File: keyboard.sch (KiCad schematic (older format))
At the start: 65 parts, among them J1 USB_A, SW1 KEY_ESC, SW10 KEY_LSPECIAL, SW11 KEY_2, SW12 KEY_W, SW13 KEY_S, SW14 KEY_X, SW15 KEY_LALT, SW16 KEY_3, SW17 KEY_E, SW18 KEY_D, SW19 KEY_C, SW2 KEY_TAB, SW20 KEY_SPACE, SW21 KEY_4, SW22 KEY_R, SW23 KEY_F, SW24 KEY_V, SW25 KEY_RALT, SW26 KEY_5, SW27 KEY_T, SW28 KEY_G, SW29 KEY_B, SW3 KEY_CAPS, SW30 KEY_RSPECIAL, SW31 KEY_6, SW32 KEY_Y, SW33 KEY_H, SW34 KEY_N, SW35 KEY_FN, SW36 KEY_7, SW37 KEY_U, SW38 KEY_J, SW39 KEY_M, SW4 KEY_LSHIFT, SW40 KEY_RCTRL, SW41 KEY_8, SW42 KEY_I, SW43 KEY_K, SW44 KEY_COMMA, SW45 KEY_9, SW46 KEY_O, SW47 KEY_L, SW48 KEY_PERIOD, SW49 KEY_0, SW5 KEY_LCTRL, SW50 KEY_P, SW51 KEY_SEMI, SW52 KEY_SLASH, SW53 KEY_MINUS, SW54 KEY_LBRACK, SW55 KEY_APOS, SW56 KEY_RSHIFT, SW57 KEY_EQUAL, SW58 KEY_RBRACK, SW59 KEY_ENTER, SW6 KEY_1, SW60 KEY_BKSPACE, SW61 KEY_BKSLSH, SW7 KEY_Q, SW8 KEY_A, SW9 KEY_Z, Y1 16mhz

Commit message: More routing
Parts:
- removed SW1: KEY_ESC, symbol CHERRYMX
- removed SW10: KEY_LSPECIAL, symbol CHERRYMX
- removed SW11: KEY_2, symbol CHERRYMX
- removed SW12: KEY_W, symbol CHERRYMX
- removed SW13: KEY_S, symbol CHERRYMX
- removed SW14: KEY_X, symbol CHERRYMX
- removed SW15: KEY_LALT, symbol CHERRYMX
- removed SW16: KEY_3, symbol CHERRYMX
- removed SW17: KEY_E, symbol CHERRYMX
- removed SW18: KEY_D, symbol CHERRYMX
- removed SW19: KEY_C, symbol CHERRYMX
- removed SW2: KEY_TAB, symbol CHERRYMX
- removed SW20: KEY_SPACE, symbol CHERRYMX
- removed SW21: KEY_4, symbol CHERRYMX
- removed SW22: KEY_R, symbol CHERRYMX
- removed SW23: KEY_F, symbol CHERRYMX
- removed SW24: KEY_V, symbol CHERRYMX
- removed SW25: KEY_RALT, symbol CHERRYMX
- removed SW26: KEY_5, symbol CHERRYMX
- removed SW27: KEY_T, symbol CHERRYMX
- removed SW28: KEY_G, symbol CHERRYMX
- removed SW29: KEY_B, symbol CHERRYMX
- removed SW3: KEY_CAPS, symbol CHERRYMX
- removed SW30: KEY_RSPECIAL, symbol CHERRYMX
- removed SW31: KEY_6, symbol CHERRYMX
- removed SW32: KEY_Y, symbol CHERRYMX
- removed SW33: KEY_H, symbol CHERRYMX
- removed SW34: KEY_N, symbol CHERRYMX
- removed SW35: KEY_FN, symbol CHERRYMX
- removed SW36: KEY_7, symbol CHERRYMX
- removed SW37: KEY_U, symbol CHERRYMX
- removed SW38: KEY_J, symbol CHERRYMX
- removed SW39: KEY_M, symbol CHERRYMX
- removed SW4: KEY_LSHIFT, symbol CHERRYMX
- removed SW40: KEY_RCTRL, symbol CHERRYMX
- removed SW41: KEY_8, symbol CHERRYMX
- removed SW42: KEY_I, symbol CHERRYMX
- removed SW43: KEY_K, symbol CHERRYMX
- removed SW44: KEY_COMMA, symbol CHERRYMX
- removed SW45: KEY_9, symbol CHERRYMX
- removed SW46: KEY_O, symbol CHERRYMX
- removed SW47: KEY_L, symbol CHERRYMX
- removed SW48: KEY_PERIOD, symbol CHERRYMX
- removed SW49: KEY_0, symbol CHERRYMX
- removed SW5: KEY_LCTRL, symbol CHERRYMX
- removed SW50: KEY_P, symbol CHERRYMX
- removed SW51: KEY_SEMI, symbol CHERRYMX
- removed SW52: KEY_SLASH, symbol CHERRYMX
- removed SW53: KEY_MINUS, symbol CHERRYMX
- removed SW54: KEY_LBRACK, symbol CHERRYMX
- removed SW55: KEY_APOS, symbol CHERRYMX
- removed SW56: KEY_RSHIFT, symbol CHERRYMX
- removed SW57: KEY_EQUAL, symbol CHERRYMX
- removed SW58: KEY_RBRACK, symbol CHERRYMX
- removed SW59: KEY_ENTER, symbol CHERRYMX
- removed SW6: KEY_1, symbol CHERRYMX
- removed SW60: KEY_BKSPACE, symbol CHERRYMX
- removed SW61: KEY_BKSLSH, symbol CHERRYMX
- removed SW7: KEY_Q, symbol CHERRYMX
- removed SW8: KEY_A, symbol CHERRYMX
- removed SW9: KEY_Z, symbol CHERRYMX
- added C3: C, Capacitors_THT:C_Rect_L4.6mm_W2.0mm_P2.50mm_MKS02_FKP02, symbol C
- added J1: CONN_01X05, Pin_Headers:Pin_Header_Straight_1x05_Pitch2.54mm, symbol CONN_01X05
- added J3: CONN_02X03, Pin_Headers:Pin_Header_Straight_2x03_Pitch2.54mm, symbol CONN_02X03
- added R1, R4: 10k, Resistors_THT:R_Axial_DIN0207_L6.3mm_D2.5mm_P10.16mm_Horizontal, symbol R
- added R2, R3: 22, Resistors_THT:R_Axial_DIN0207_L6.3mm_D2.5mm_P10.16mm_Horizontal, symbol R_Small
- added U1: ATMEGA32U4-AU, Housings_QFP:TQFP-44_10x10mm_Pitch0.8mm, symbol ATMEGA32U4-AU
- C1, C2: footprint (none) -> Capacitors_THT:C_Rect_L4.6mm_W2.0mm_P2.50mm_MKS02_FKP02
- J2: renamed from J1; footprint (none) -> Connectors:USB_A
- Y1: footprint (none) -> Crystals:Crystal_HC49-4H_Vertical
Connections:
- net GND: now also J2.4 (GND), J2.5 (Shield), C3.2, J1.4 (P4), J3.6 (P6), R4.2, U1.15 (GND), U1.23 (GND), U1.35 (GND), U1.43 (GND), U1.5 (UGND)
- net at C1.2, Y1.1: now also U1.17 (XTAL1)
- net at C2.2, Y1.2: now also U1.16 (XTAL2)
- net VCC: now reaches J2.1 (VBUS)
- net VCC: now also J1.5 (P5), J3.2 (P2), R1.1, U1.14 (VCC), U1.2 (UVCC), U1.24 (AVCC), U1.34 (VCC), U1.44 (AVCC), U1.7 (VBUS)
- net at J2.2 (D-): now also R3.2
- net at J2.3 (D+): now also R2.1
- new net: R3.1, U1.3 (D-)
- new net: R4.1, U1.33 ((~HWB~)PE2)
- new net: R2.2, U1.4 (D+)
- new net: C3.1, U1.6 (UCAP)
- new net EXT1: J1.1 (P1), U1.41 ((ADC0)PF0)
- new net EXT2: J1.2 (P2), U1.40 ((ADC1)PF1)
- new net EXT3: J1.3 (P3), U1.39 ((ADC4/TCK)PF4)
- new net MISO: J3.1 (P1), U1.11 ((PDO/MISO/PCINT3)PB3)
- new net MOSI: J3.4 (P4), U1.10 ((PDI/MOSI/PCINT2)PB2)
- new net RES: R1.2, U1.13 (~RESET~)
- new net RST: J3.5 (P5)
- new net SCK: J3.3 (P3), U1.9 ((SCLK/PCINT1)PB1)
- new net matrix/col1: U1.29 ((ADC12/OC1A/~OC4B~/PCINT12)PB5)
- new net matrix/col10: U1.25 ((ICP2/ADC8)PD4)
- new net matrix/col11: U1.22 ((XCK1/~CTS~)PD5)
- new net matrix/col12: U1.26 ((T1/~OC4D~/ADC9)PD6)
- new net matrix/col13: U1.27 ((T0/OC4D/ADC10)PD7)
- new net matrix/col14: U1.1 ((INT6/AIN0)PE6)
- new net matrix/col2: U1.30 ((ADC13/OC1B/OC4B/PCINT13)PB6)
- new net matrix/col3: U1.12 ((OC0A/OC1C/~RTS~/PCINT7)PB7)
- new net matrix/col4: U1.31 ((OC3A/~OC4A~)PC6)
- new net matrix/col5: U1.32 ((ICP3/CLK0/OC4A)PC7)
- new net matrix/col6: U1.18 ((OC0B/SCL/INT0)PD0)
- new net matrix/col7: U1.19 ((SDA/INT1)PD1)
- new net matrix/col8: U1.20 ((RXD/INT2)PD2)
- new net matrix/col9: U1.21 ((TXD/INT3)PD3)
- new net matrix/row1: U1.8 ((SS/PCINT0)PB0)
- new net matrix/row5: U1.28 ((ADC11/PCINT4)PB4)
- no-connect marks 0 -> 4
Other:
- moved on the sheet: C1, C2, J2, Y1

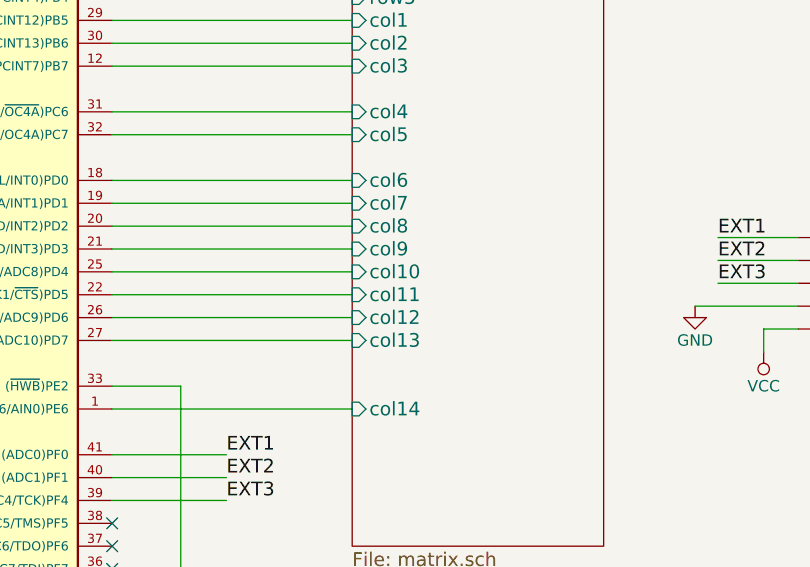
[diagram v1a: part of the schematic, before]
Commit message: switch col 10 and 11
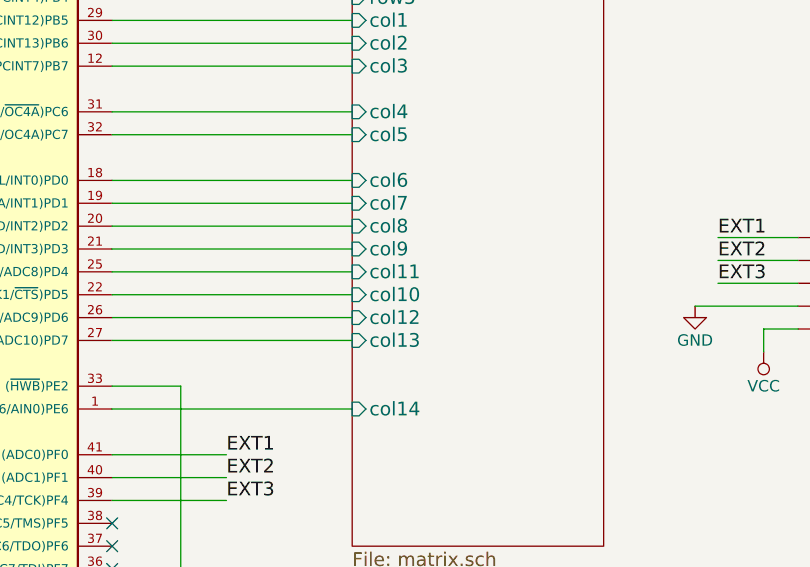
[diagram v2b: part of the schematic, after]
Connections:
- net matrix/col10: now also U1.22 ((XCK1/~CTS~)PD5); no longer U1.25 ((ICP2/ADC8)PD4)
- net matrix/col11: now also U1.25 ((ICP2/ADC8)PD4); no longer U1.22 ((XCK1/~CTS~)PD5)
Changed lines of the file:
@@
 F14 "col8" I L 9450 2900 60
 F15 "col9" I L 9450 3000 60
-F16 "col10" I L 9450 3100 60
-F17 "col11" I L 9450 3200 60
+F16 "col10" I L 9450 3200 60
+F17 "col11" I L 9450 3100 60
 F18 "col12" I L 9450 3300 60
 F19 "col13" I L 9450 3400 60

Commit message: more routing
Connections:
- net matrix/col5: now also U1.8 ((SS/PCINT0)PB0); no longer U1.32 ((ICP3/CLK0/OC4A)PC7)
- net matrix/row1: now also U1.32 ((ICP3/CLK0/OC4A)PC7); no longer U1.8 ((SS/PCINT0)PB0)
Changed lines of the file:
@@
 F0 "matrix" 60
 F1 "matrix.sch" 60
-F2 "row1" I L 9450 1500 60
+F2 "row1" I L 9450 2500 60
 F3 "row2" I L 9450 1600 60
 F4 "row3" I L 9450 1700 60
@@
 F9 "col3" I L 9450 2200 60
 F10 "col4" I L 9450 2400 60
-F11 "col5" I L 9450 2500 60
+F11 "col5" I L 9450 1500 60
 F12 "col6" I L 9450 2700 60
 F13 "col7" I L 9450 2800 60

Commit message: almost done
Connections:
- net matrix/col1: now also U1.31 ((OC3A/~OC4A~)PC6); no longer U1.29 ((ADC12/OC1A/~OC4B~/PCINT12)PB5)
- net matrix/col14: now also U1.29 ((ADC12/OC1A/~OC4B~/PCINT12)PB5); no longer U1.1 ((INT6/AIN0)PE6)
- net matrix/col3: now also U1.1 ((INT6/AIN0)PE6); no longer U1.12 ((OC0A/OC1C/~RTS~/PCINT7)PB7)
- net matrix/col4: now also U1.8 ((SS/PCINT0)PB0); no longer U1.31 ((OC3A/~OC4A~)PC6)
- net matrix/col5: now also U1.12 ((OC0A/OC1C/~RTS~/PCINT7)PB7); no longer U1.8 ((SS/PCINT0)PB0)
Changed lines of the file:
@@
 F5 "row4" I L 9450 1800 60
 F6 "row5" I L 9450 1900 60
-F7 "col1" I L 9450 2000 60
+F7 "col1" I L 9450 2400 60
 F8 "col2" I L 9450 2100 60
-F9 "col3" I L 9450 2200 60
-F10 "col4" I L 9450 2400 60
-F11 "col5" I L 9450 1500 60
+F9 "col3" I L 9450 3700 60
+F10 "col4" I L 9450 1500 60
+F11 "col5" I L 9450 2200 60
 F12 "col6" I L 9450 2700 60
 F13 "col7" I L 9450 2800 60
@@
 F18 "col12" I L 9450 3300 60
 F19 "col13" I L 9450 3400 60
-F20 "col14" I L 9450 3700 60
+F20 "col14" I L 9450 2000 60
 $EndSheet
 $Comp

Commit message: fab
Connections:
- net RES is gone; now on net RST: R1.2, U1.13 (~RESET~)
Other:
- moved on the sheet: J3
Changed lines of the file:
@@
-$EndComp
-$Comp
-L GND #PWR02
-U 1 1 59167107
-P 12300 8700
-F 0 "#PWR02" H 12300 8450 50  0001 C CNN
-F 1 "GND" H 12300 8550 50  0000 C CNN
-F 2 "" H 12300 8700 50  0001 C CNN
-F 3 "" H 12300 8700 50  0001 C CNN
-	1    12300 8700
-	1    0    0    -1
 $EndComp
 $Comp
@@
 $EndComp
 $Comp
-L GND #PWR03
+L GND #PWR02
 U 1 1 5922F8E2
 P 3500 3400
-F 0 "#PWR03" H 3500 3150 50  0001 C CNN
+F 0 "#PWR02" H 3500 3150 50  0001 C CNN
 F 1 "GND" H 3500 3250 50  0000 C CNN
 F 2 "" H 3500 3400 50  0001 C CNN
@@
 $EndComp
 $Comp
-L VCC #PWR04
+L VCC #PWR03
 U 1 1 5922FA55
 P 3800 2500
-F 0 "#PWR04" H 3800 2350 50  0001 C CNN
+F 0 "#PWR03" H 3800 2350 50  0001 C CNN
 F 1 "VCC" H 3800 2650 50  0000 C CNN
 F 2 "" H 3800 2500 50  0001 C CNN
@@
 $EndComp
 $Comp
-L GND #PWR05
+L GND #PWR04
 U 1 1 592321DB
 P 5950 3600
-F 0 "#PWR05" H 5950 3350 50  0001 C CNN
+F 0 "#PWR04" H 5950 3350 50  0001 C CNN
 F 1 "GND" H 5950 3450 50  0000 C CNN
 F 2 "" H 5950 3600 50  0001 C CNN
@@
 $EndComp
 $Comp
-L VCC #PWR06
+L VCC #PWR05
 U 1 1 59232414
 P 6500 1150
-F 0 "#PWR06" H 6500 1000 50  0001 C CNN
+F 0 "#PWR05" H 6500 1000 50  0001 C CNN
 F 1 "VCC" H 6500 1300 50  0000 C CNN
 F 2 "" H 6500 1150 50  0001 C CNN
@@
 $EndComp
 $Comp
-L GND #PWR07
+L GND #PWR06
 U 1 1 59233079
 P 6800 4800
-F 0 "#PWR07" H 6800 4550 50  0001 C CNN
+F 0 "#PWR06" H 6800 4550 50  0001 C CNN
 F 1 "GND" H 6800 4650 50  0000 C CNN
 F 2 "" H 6800 4800 50  0001 C CNN
@@
 $EndComp
 $Comp
-L VCC #PWR08
+L VCC #PWR07
 U 1 1 59234354
 P 5700 900
-F 0 "#PWR08" H 5700 750 50  0001 C CNN
+F 0 "#PWR07" H 5700 750 50  0001 C CNN
 F 1 "VCC" H 5700 1050 50  0000 C CNN
 F 2 "" H 5700 900 50  0001 C CNN
@@
 $EndComp
 $Comp
-L VCC #PWR09
+L VCC #PWR08
 U 1 1 59238A80
 P 6050 2600
-F 0 "#PWR09" H 6050 2450 50  0001 C CNN
+F 0 "#PWR08" H 6050 2450 50  0001 C CNN
 F 1 "VCC" H 6050 2750 50  0000 C CNN
 F 2 "" H 6050 2600 50  0001 C CNN
@@
 L CONN_02X03 J3
 U 1 1 5923A26D
-P 10950 5500
-F 0 "J3" H 10950 5700 50  0000 C CNN
-F 1 "CONN_02X03" H 10950 5300 50  0000 C CNN
-F 2 "Pin_Headers:Pin_Header_Straight_2x03_Pitch2.54mm" H 10950 4300 50  0001 C CNN
-F 3 "" H 10950 4300 50  0001 C CNN
-	1    10950 5500
-	1    0    0    -1
-$EndComp
-Text Label 6000 950  0    60   ~ 0
-RES
-Text Label 10200 5600 0    60   ~ 0
+P 10200 4900
+F 0 "J3" H 10200 5100 50  0000 C CNN
+F 1 "CONN_02X03" H 10200 4700 50  0000 C CNN
+F 2 "Pin_Headers:Pin_Header_Straight_2x03_Pitch2.54mm" H 10200 3700 50  0001 C CNN
+F 3 "" H 10200 3700 50  0001 C CNN
+	1    10200 4900
+	1    0    0    -1
+$EndComp
+Text Label 5950 1500 0    60   ~ 0
 RST
-Text Label 10200 5500 0    60   ~ 0
+Text Label 9450 5000 0    60   ~ 0
+RST
+Text Label 9450 4900 0    60   ~ 0
 SCK
-Text Label 10200 5400 0    60   ~ 0
+Text Label 9450 4800 0    60   ~ 0
 MISO
 $Comp
-L VCC #PWR010
+L VCC #PWR09
 U 1 1 5923BAB5
-P 11700 5200
-F 0 "#PWR010" H 11700 5050 50  0001 C CNN
-F 1 "VCC" H 11700 5350 50  0000 C CNN
-F 2 "" H 11700 5200 50  0001 C CNN
-F 3 "" H 11700 5200 50  0001 C CNN
-	1    11700 5200
-	1    0    0    -1
-$EndComp
-$Comp
-L GND #PWR011
+P 10950 4600
+F 0 "#PWR09" H 10950 4450 50  0001 C CNN
+F 1 "VCC" H 10950 4750 50  0000 C CNN
+F 2 "" H 10950 4600 50  0001 C CNN
+F 3 "" H 10950 4600 50  0001 C CNN
+	1    10950 4600
+	1    0    0    -1
+$EndComp
+$Comp
+L GND #PWR010
 U 1 1 5923BC2F
-P 11700 5800
-F 0 "#PWR011" H 11700 5550 50  0001 C CNN
-F 1 "GND" H 11700 5650 50  0000 C CNN
-F 2 "" H 11700 5800 50  0001 C CNN
-F 3 "" H 11700 5800 50  0001 C CNN
-	1    11700 5800
-	1    0    0    -1
-$EndComp
-Text Label 11700 5500 0    60   ~ 0
+P 10950 5200
+F 0 "#PWR010" H 10950 4950 50  0001 C CNN
+F 1 "GND" H 10950 5050 50  0000 C CNN
+F 2 "" H 10950 5200 50  0001 C CNN
+F 3 "" H 10950 5200 50  0001 C CNN
+	1    10950 5200
+	1    0    0    -1
+$EndComp
+Text Label 10950 4900 0    60   ~ 0
 MOSI
 Text Label 8500 1700 0    60   ~ 0
@@
 $EndComp
 $Comp
-L GND #PWR012
+L GND #PWR011
 U 1 1 5923D907
 P 8700 5200
-F 0 "#PWR012" H 8700 4950 50  0001 C CNN
+F 0 "#PWR011" H 8700 4950 50  0001 C CNN
 F 1 "GND" H 8700 5050 50  0000 C CNN
 F 2 "" H 8700 5200 50  0001 C CNN
@@
 EXT3
 $Comp
+L PWR_FLAG #FLG012
+U 1 1 59245AFA
+P 3650 1450
+F 0 "#FLG012" H 3650 1525 50  0001 C CNN
+F 1 "PWR_FLAG" H 3650 1600 50  0000 C CNN
+F 2 "" H 3650 1450 50  0001 C CNN
+F 3 "" H 3650 1450 50  0001 C CNN
+	1    3650 1450
+	1    0    0    -1
+$EndComp
+$Comp
 L PWR_FLAG #FLG013
-U 1 1 59245AFA
-P 3350 1250
-F 0 "#FLG013" H 3350 1325 50  0001 C CNN
-F 1 "PWR_FLAG" H 3350 1400 50  0000 C CNN
-F 2 "" H 3350 1250 50  0001 C CNN
-F 3 "" H 3350 1250 50  0001 C CNN
-	1    3350 1250
-	1    0    0    -1
-$EndComp
-$Comp
-L PWR_FLAG #FLG014
 U 1 1 59245BDD
-P 3850 1250
-F 0 "#FLG014" H 3850 1325 50  0001 C CNN
-F 1 "PWR_FLAG" H 3850 1400 50  0000 C CNN
-F 2 "" H 3850 1250 50  0001 C CNN
-F 3 "" H 3850 1250 50  0001 C CNN
-	1    3850 1250
-	1    0    0    -1
-$EndComp
-$Comp
-L VCC #PWR015
+P 4150 1450
+F 0 "#FLG013" H 4150 1525 50  0001 C CNN
+F 1 "PWR_FLAG" H 4150 1600 50  0000 C CNN
+F 2 "" H 4150 1450 50  0001 C CNN
+F 3 "" H 4150 1450 50  0001 C CNN
+	1    4150 1450
+	1    0    0    -1
+$EndComp
+$Comp
+L VCC #PWR014
 U 1 1 59245CC0
-P 3350 1400
-F 0 "#PWR015" H 3350 1250 50  0001 C CNN
-F 1 "VCC" H 3350 1550 50  0000 C CNN
-F 2 "" H 3350 1400 50  0001 C CNN
-F 3 "" H 3350 1400 50  0001 C CNN
-	1    3350 1400
+P 3650 1600
+F 0 "#PWR014" H 3650 1450 50  0001 C CNN
+F 1 "VCC" H 3650 1750 50  0000 C CNN
+F 2 "" H 3650 1600 50  0001 C CNN
+F 3 "" H 3650 1600 50  0001 C CNN
+	1    3650 1600
 	-1   0    0    1
 $EndComp
 $Comp
-L GND #PWR016
+L GND #PWR015
 U 1 1 59245DA3
-P 3850 1400
-F 0 "#PWR016" H 3850 1150 50  0001 C CNN
-F 1 "GND" H 3850 1250 50  0000 C CNN
-F 2 "" H 3850 1400 50  0001 C CNN
-F 3 "" H 3850 1400 50  0001 C CNN
-	1    3850 1400
+P 4150 1600
+F 0 "#PWR015" H 4150 1350 50  0001 C CNN
+F 1 "GND" H 4150 1450 50  0000 C CNN
+F 2 "" H 4150 1600 50  0001 C CNN
+F 3 "" H 4150 1600 50  0001 C CNN
+	1    4150 1600
 	1    0    0    -1
 $EndComp
@@
 $EndComp
 $Comp
-L GND #PWR017
+L GND #PWR016
 U 1 1 5921F590
 P 10950 3250
-F 0 "#PWR017" H 10950 3000 50  0001 C CNN
+F 0 "#PWR016" H 10950 3000 50  0001 C CNN
 F 1 "GND" H 10950 3100 50  0000 C CNN
 F 2 "" H 10950 3250 50  0001 C CNN
@@
 $EndComp
 $Comp
-L VCC #PWR018
+L VCC #PWR017
 U 1 1 5921F676
 P 11250 3450
-F 0 "#PWR018" H 11250 3300 50  0001 C CNN
+F 0 "#PWR017" H 11250 3300 50  0001 C CNN
 F 1 "VCC" H 11250 3600 50  0000 C CNN
 F 2 "" H 11250 3450 50  0001 C CNN
@@
 Connection ~ 5150 2200
 Wire Wire Line
-	12450 8450 12300 8450
-Wire Wire Line
-	12300 8450 12300 8700
-Wire Wire Line
-	12450 8550 12300 8550
-Connection ~ 12300 8550
-Wire Wire Line
 	3300 3250 3300 3300
 Wire Wire Line
@@
 	6050 2700 6050 2600
 Wire Wire Line
-	6000 1500 6000 950
-Connection ~ 6000 1500
-Wire Wire Line
-	10700 5600 10200 5600
-Wire Wire Line
-	10700 5500 10200 5500
-Wire Wire Line
-	10200 5400 10700 5400
-Wire Wire Line
-	11200 5400 11700 5400
-Wire Wire Line
-	11700 5400 11700 5200
-Wire Wire Line
-	11200 5600 11700 5600
-Wire Wire Line
-	11700 5600 11700 5800
-Wire Wire Line
-	11200 5500 11700 5500
+	9950 5000 9450 5000
+Wire Wire Line
+	9950 4900 9450 4900
+Wire Wire Line
+	9450 4800 9950 4800
+Wire Wire Line
+	10450 4800 10950 4800
+Wire Wire Line
+	10950 4800 10950 4600
+Wire Wire Line
+	10450 5000 10950 5000
+Wire Wire Line
+	10950 5000 10950 5200
+Wire Wire Line
+	10450 4900 10950 4900
 Wire Wire Line
 	8400 1700 9450 1700
@@
 	8400 4100 8900 4100
 Wire Wire Line
-	5700 1500 6150 1500
-Wire Wire Line
-	3850 1250 3850 1400
-Wire Wire Line
-	3350 1250 3350 1400
+	4150 1450 4150 1600
+Wire Wire Line
+	3650 1450 3650 1600
 Wire Wire Line
 	11400 3350 11250 3350
@@
 Text Label 11050 3150 0    60   ~ 0
 EXT3
+Wire Wire Line
+	6150 1500 5700 1500
 $EndSCHEMATC
